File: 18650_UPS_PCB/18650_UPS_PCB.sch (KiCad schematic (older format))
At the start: 59 parts, among them J1 USB_B_Micro, J2 Conn_02x04_Odd_Even, J3 USB_A, SW1 SW_SPDT, SW2 ALPSALPINE_SKRHADE011, SW3 SW_SPDT, SW4 SW_SPDT, SW5 SW_SPDT, U1 STLINK-V3MINI, U10 LR9102G-xx, U2 R5478, U3 STC4054, U4 FS8205A, U5 ME2188Cxx, U6 XC9236Axx, U7 INA219AxD, U8 SSD1306_128_32, U9 STM32F030F4Px

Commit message: all components on board
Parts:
- removed TP1, TP2, TP3, TP4, TP5: TestPoint, TestPoint:TestPoint_Keystone_5015_Micro-Minature, symbol Connector:TestPoint
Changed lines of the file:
@@
 	6700 8300 6600 8300
-Wire Wire Line
-	6600 8950 6600 9000
 Wire Wire Line
 	6700 7900 6600 7900
@@
 Wire Wire Line
 	7300 5950 8200 5950
-Wire Wire Line
-	6600 9350 6600 9400
 $Comp
 L power:-BATT #PWR015
@@
 $EndComp
 $Comp
-L power:+5V #PWR027
-U 1 1 60E79ACF
-P 13350 5800
-AR Path="/60E79ACF" Ref="#PWR027"  Part="1"
-AR Path="/60952D5B/60E79ACF" Ref="#PWR?"  Part="1"
-F 0 "#PWR027" H 13350 5650 50  0001 C CNN
-F 1 "+5V" H 13365 5973 50  0000 C CNN
-F 2 "" H 13350 5800 50  0001 C CNN
-F 3 "" H 13350 5800 50  0001 C CNN
-	1    13350 5800
-	1    0    0    -1
-$EndComp
-$Comp
 L power:GNDD #PWR025
 U 1 1 60E79E71
@@
 	13250 5900 13350 5900
 Connection ~ 13350 5900
-Wire Wire Line
-	13350 5900 13350 5800
 $Comp
 L power:GNDD #PWR028
@@
 Wire Wire Line
 	12000 4100 12000 4000
-$Comp
-L power:+3V3 #PWR031
-U 1 1 60F8808E
-P 13900 3700
-AR Path="/60F8808E" Ref="#PWR031"  Part="1"
-AR Path="/60952D5B/60F8808E" Ref="#PWR?"  Part="1"
-F 0 "#PWR031" H 13900 3550 50  0001 C CNN
-F 1 "+3V3" H 13915 3873 50  0000 C CNN
-F 2 "" H 13900 3700 50  0001 C CNN
-F 3 "" H 13900 3700 50  0001 C CNN
-	1    13900 3700
-	1    0    0    -1
-$EndComp
 Wire Wire Line
 	13250 3950 13350 3950
@@
 Wire Wire Line
 	11950 7950 11950 7900
-$Comp
-L power:+3.3VA #PWR029
-U 1 1 6112D4E0
-P 13700 7850
-F 0 "#PWR029" H 13700 7700 50  0001 C CNN
-F 1 "+3.3VA" H 13715 8023 50  0000 C CNN
-F 2 "" H 13700 7850 50  0001 C CNN
-F 3 "" H 13700 7850 50  0001 C CNN
-	1    13700 7850
-	1    0    0    -1
-$EndComp
-Wire Wire Line
-	13700 7950 13700 7850
 Connection ~ 13700 7950
 Wire Notes Line
@@
 	1    0    0    -1
 $EndComp
-$Comp
-L Connector:TestPoint TP1
-U 1 1 60CA037D
-P 6900 8900
-F 0 "TP1" H 6958 9018 50  0000 L CNN
-F 1 "TestPoint" H 6958 8927 50  0000 L CNN
-F 2 "TestPoint:TestPoint_Keystone_5015_Micro-Minature" H 7100 8900 50  0001 C CNN
-F 3 "~" H 7100 8900 50  0001 C CNN
-	1    6900 8900
-	1    0    0    -1
-$EndComp
-$Comp
-L Connector:TestPoint TP2
-U 1 1 60CAD6BC
-P 6900 9350
-F 0 "TP2" H 6958 9468 50  0000 L CNN
-F 1 "TestPoint" H 6958 9377 50  0000 L CNN
-F 2 "TestPoint:TestPoint_Keystone_5015_Micro-Minature" H 7100 9350 50  0001 C CNN
-F 3 "~" H 7100 9350 50  0001 C CNN
-	1    6900 9350
-	1    0    0    -1
-$EndComp
-Wire Wire Line
-	6900 9350 6900 9400
-Wire Wire Line
-	6900 9400 6600 9400
-Connection ~ 6600 9400
-Wire Wire Line
-	6600 9400 6600 9450
-Wire Wire Line
-	6900 8900 6900 9000
-Wire Wire Line
-	6900 9000 6600 9000
-Connection ~ 6600 9000
-Wire Wire Line
-	6600 9000 6600 9050
-$Comp
-L Connector:TestPoint TP4
-U 1 1 60CC539E
-P 14000 7900
-F 0 "TP4" H 14058 8018 50  0000 L CNN
-F 1 "TestPoint" H 14058 7927 50  0000 L CNN
-F 2 "TestPoint:TestPoint_Keystone_5015_Micro-Minature" H 14200 7900 50  0001 C CNN
-F 3 "~" H 14200 7900 50  0001 C CNN
-	1    14000 7900
-	1    0    0    -1
-$EndComp
-Wire Wire Line
-	13700 7950 14000 7950
-Wire Wire Line
-	14000 7950 14000 7900
-$Comp
-L Connector:TestPoint TP3
-U 1 1 60CD1FDC
-P 13650 5850
-F 0 "TP3" H 13708 5968 50  0000 L CNN
-F 1 "TestPoint" H 13708 5877 50  0000 L CNN
-F 2 "TestPoint:TestPoint_Keystone_5015_Micro-Minature" H 13850 5850 50  0001 C CNN
-F 3 "~" H 13850 5850 50  0001 C CNN
-	1    13650 5850
-	1    0    0    -1
-$EndComp
-Wire Wire Line
-	13350 5900 13650 5900
-Wire Wire Line
-	13650 5900 13650 5850
-$Comp
-L Connector:TestPoint TP5
-U 1 1 60CDED71
-P 14150 3750
-F 0 "TP5" H 14208 3868 50  0000 L CNN
-F 1 "TestPoint" H 14208 3777 50  0000 L CNN
-F 2 "TestPoint:TestPoint_Keystone_5015_Micro-Minature" H 14350 3750 50  0001 C CNN
-F 3 "~" H 14350 3750 50  0001 C CNN
-	1    14150 3750
-	1    0    0    -1
-$EndComp
-Wire Wire Line
-	13900 3700 13900 3750
 Wire Wire Line
 	13650 3750 13900 3750
@@
 Wire Wire Line
 	13900 3750 13900 3800
-Wire Wire Line
-	13900 3750 14150 3750
 $Comp
 L Connector:USB_A J3
@@
 NoConn ~ 4150 10550
 NoConn ~ 2900 10450
-$Comp
-L power:+3.3VA #PWR?
+Wire Wire Line
+	13900 3700 13900 3750
+$Comp
+L power:+3V3 #PWR031
+U 1 1 60F8808E
+P 13900 3700
+AR Path="/60F8808E" Ref="#PWR031"  Part="1"
+AR Path="/60952D5B/60F8808E" Ref="#PWR?"  Part="1"
+F 0 "#PWR031" H 13900 3550 50  0001 C CNN
+F 1 "+3V3" H 13915 3873 50  0000 C CNN
+F 2 "" H 13900 3700 50  0001 C CNN
+F 3 "" H 13900 3700 50  0001 C CNN
+	1    13900 3700
+	1    0    0    -1
+$EndComp
+Wire Wire Line
+	13350 5900 13350 5800
+$Comp
+L power:+5V #PWR027
+U 1 1 60E79ACF
+P 13350 5800
+AR Path="/60E79ACF" Ref="#PWR027"  Part="1"
+AR Path="/60952D5B/60E79ACF" Ref="#PWR?"  Part="1"
+F 0 "#PWR027" H 13350 5650 50  0001 C CNN
+F 1 "+5V" H 13365 5973 50  0000 C CNN
+F 2 "" H 13350 5800 50  0001 C CNN
+F 3 "" H 13350 5800 50  0001 C CNN
+	1    13350 5800
+	1    0    0    -1
+$EndComp
+$Comp
+L power:+3.3VA #PWR0110
 U 1 1 61291B27
 P 2150 4850
-F 0 "#PWR?" H 2150 4700 50  0001 C CNN
+F 0 "#PWR0110" H 2150 4700 50  0001 C CNN
 F 1 "+3.3VA" H 2165 5023 50  0000 C CNN
 F 2 "" H 2150 4850 50  0001 C CNN
@@
 	1    0    0    -1
 $EndComp
+Wire Wire Line
+	13700 7950 13700 7850
+$Comp
+L power:+3.3VA #PWR029
+U 1 1 6112D4E0
+P 13700 7850
+F 0 "#PWR029" H 13700 7700 50  0001 C CNN
+F 1 "+3.3VA" H 13715 8023 50  0000 C CNN
+F 2 "" H 13700 7850 50  0001 C CNN
+F 3 "" H 13700 7850 50  0001 C CNN
+	1    13700 7850
+	1    0    0    -1
+$EndComp
+Wire Wire Line
+	6600 9350 6600 9450
+Wire Wire Line
+	6600 8950 6600 9050
 $EndSCHEMATC

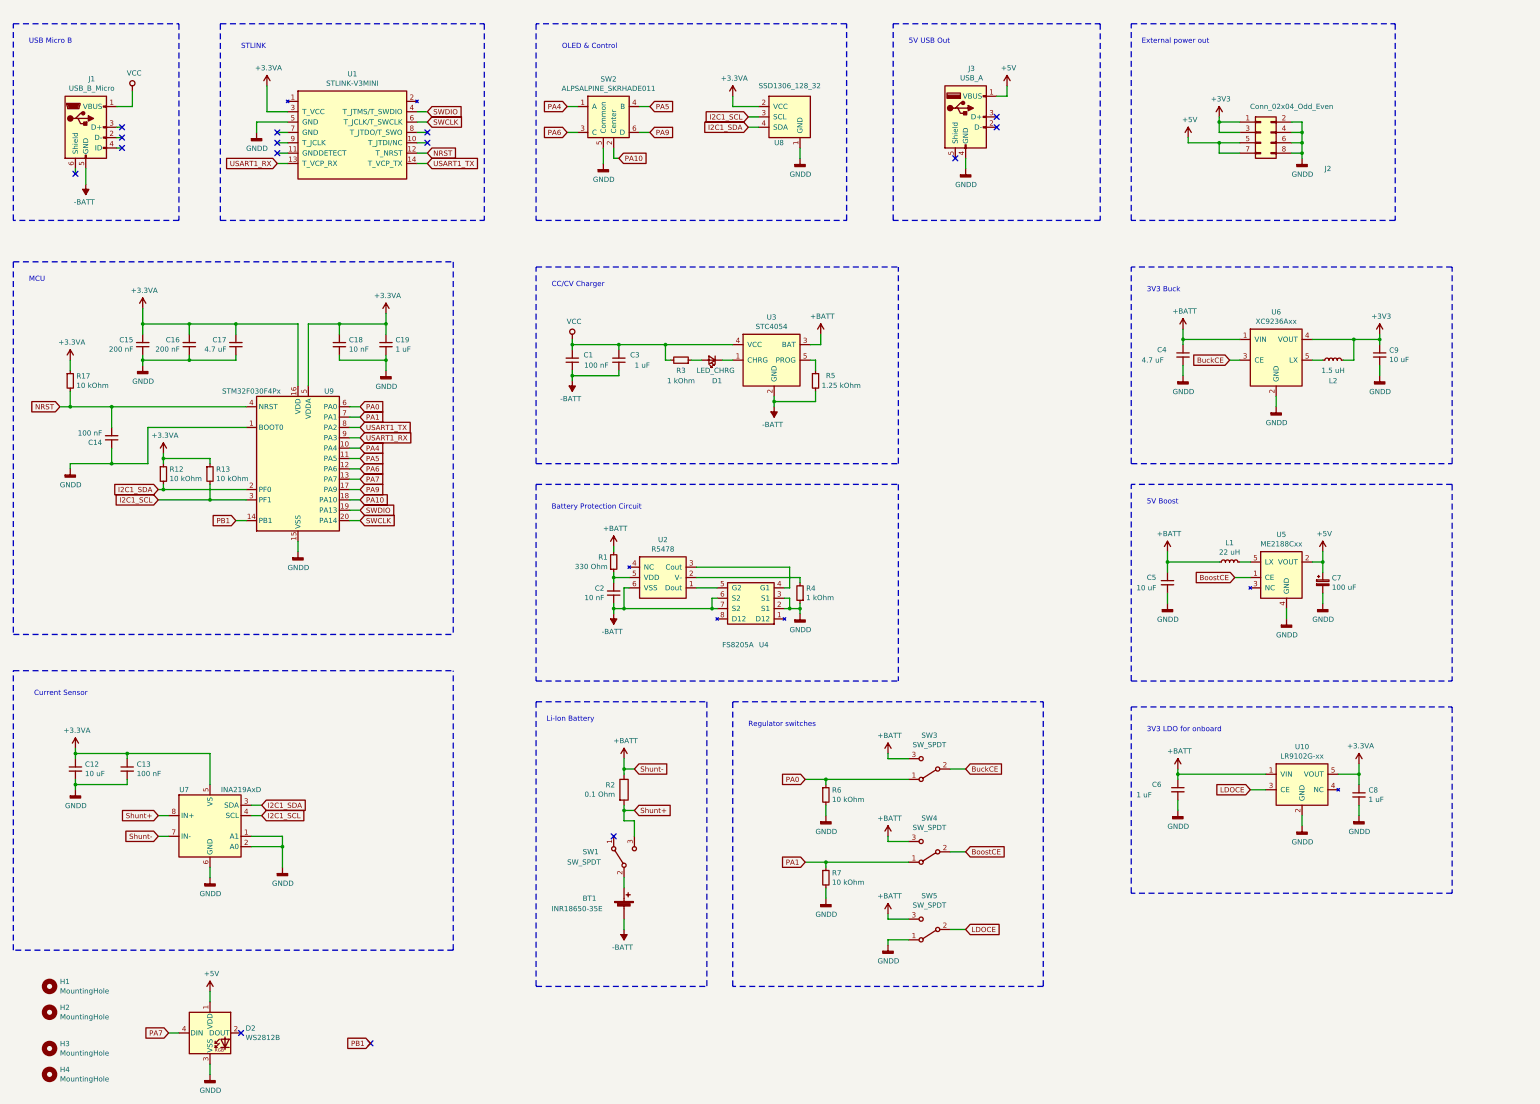
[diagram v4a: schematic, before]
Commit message: v2 layout complete and started routing
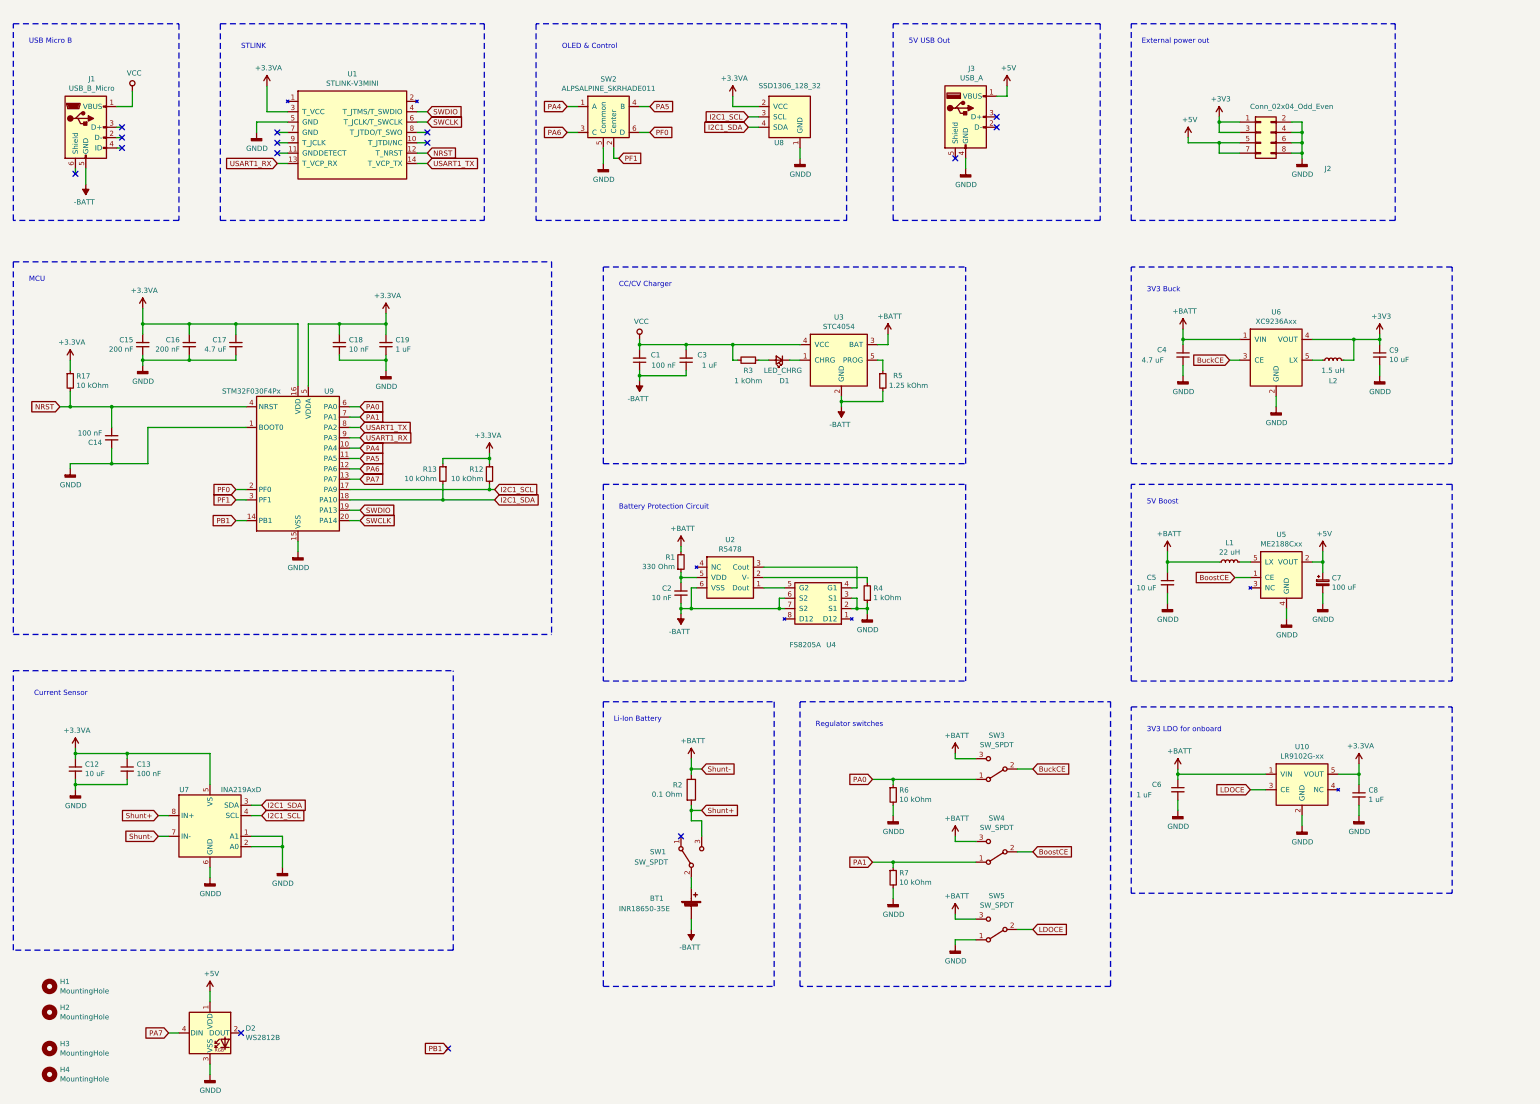
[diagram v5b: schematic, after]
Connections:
- net I2C1_SCL: now also R12.2, U9.17 (PA9); no longer R13.2, U9.3 (PF1)
- net I2C1_SDA: now also R13.2, U9.18 (PA10); no longer R12.2, U9.2 (PF0)
- net PA10 renamed PF1
- net PF1: now also U9.3 (PF1); no longer U9.18 (PA10)
- net PA9 renamed PF0
- net PF0: now also U9.2 (PF0); no longer U9.17 (PA9)
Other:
- moved on the sheet: BT1, C1, C2, C3, D1, R1, R12, R13, R2, R3, R4, R5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

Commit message: routing
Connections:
- net PA0: now also R7.1, SW4.1 (A); no longer R6.1, SW3.1 (A)
- net PA1: now also R6.1, SW3.1 (A); no longer R7.1, SW4.1 (A)
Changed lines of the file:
@@
 Text GLabel 6050 1750 0    50   Input ~ 0
 PA6
+Text GLabel 9000 8800 0    50   Input ~ 0
+PA0
 Text GLabel 9000 8000 0    50   Input ~ 0
-PA0
-Text GLabel 9000 8800 0    50   Input ~ 0
 PA1
 Text GLabel 10550 7900 2    50   Input ~ 0

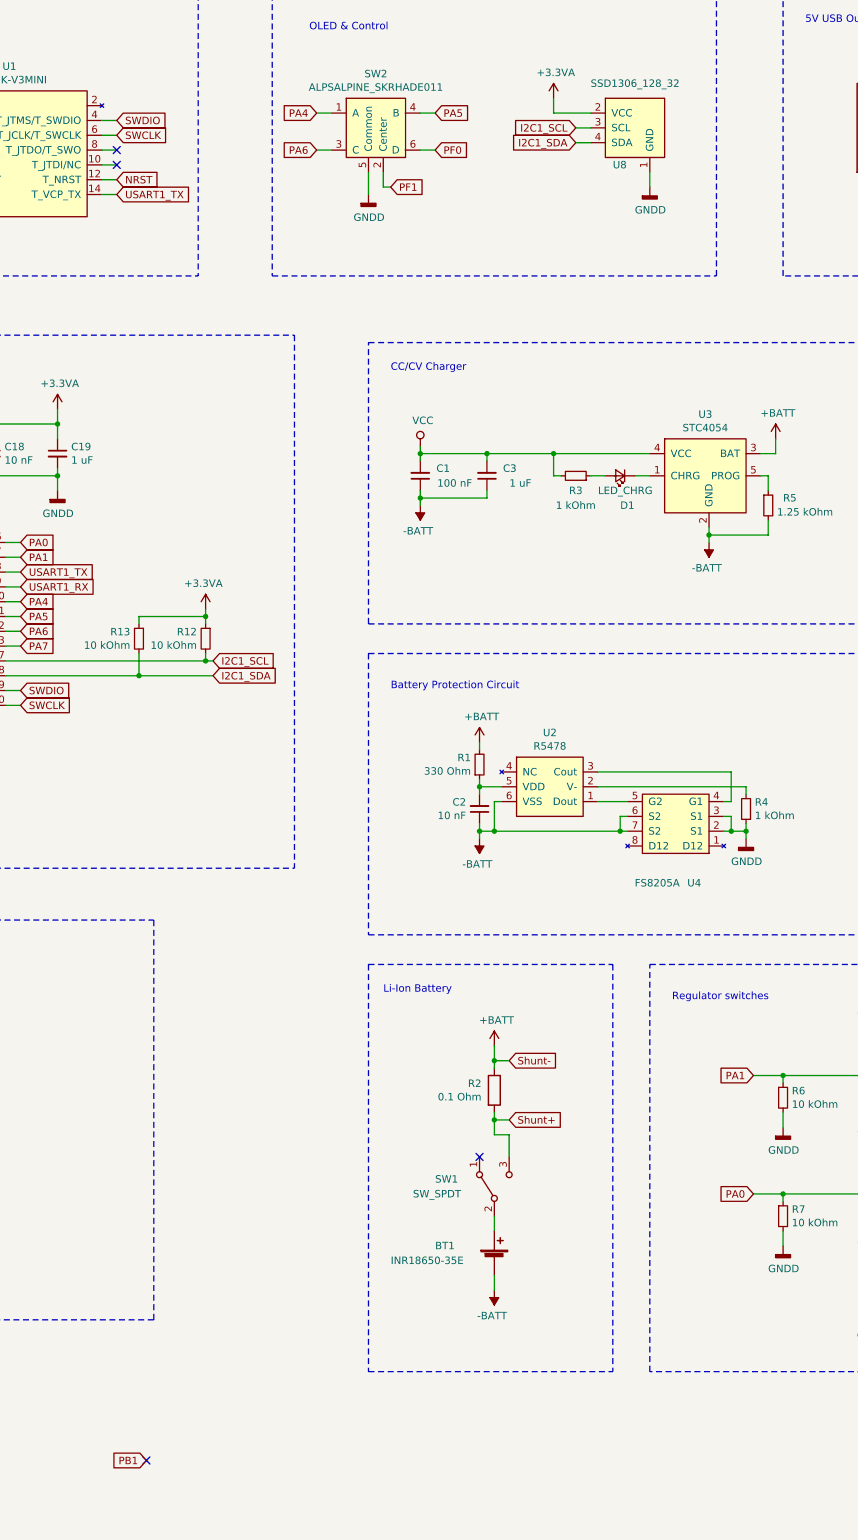
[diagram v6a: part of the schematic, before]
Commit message: cleaned routing significantly
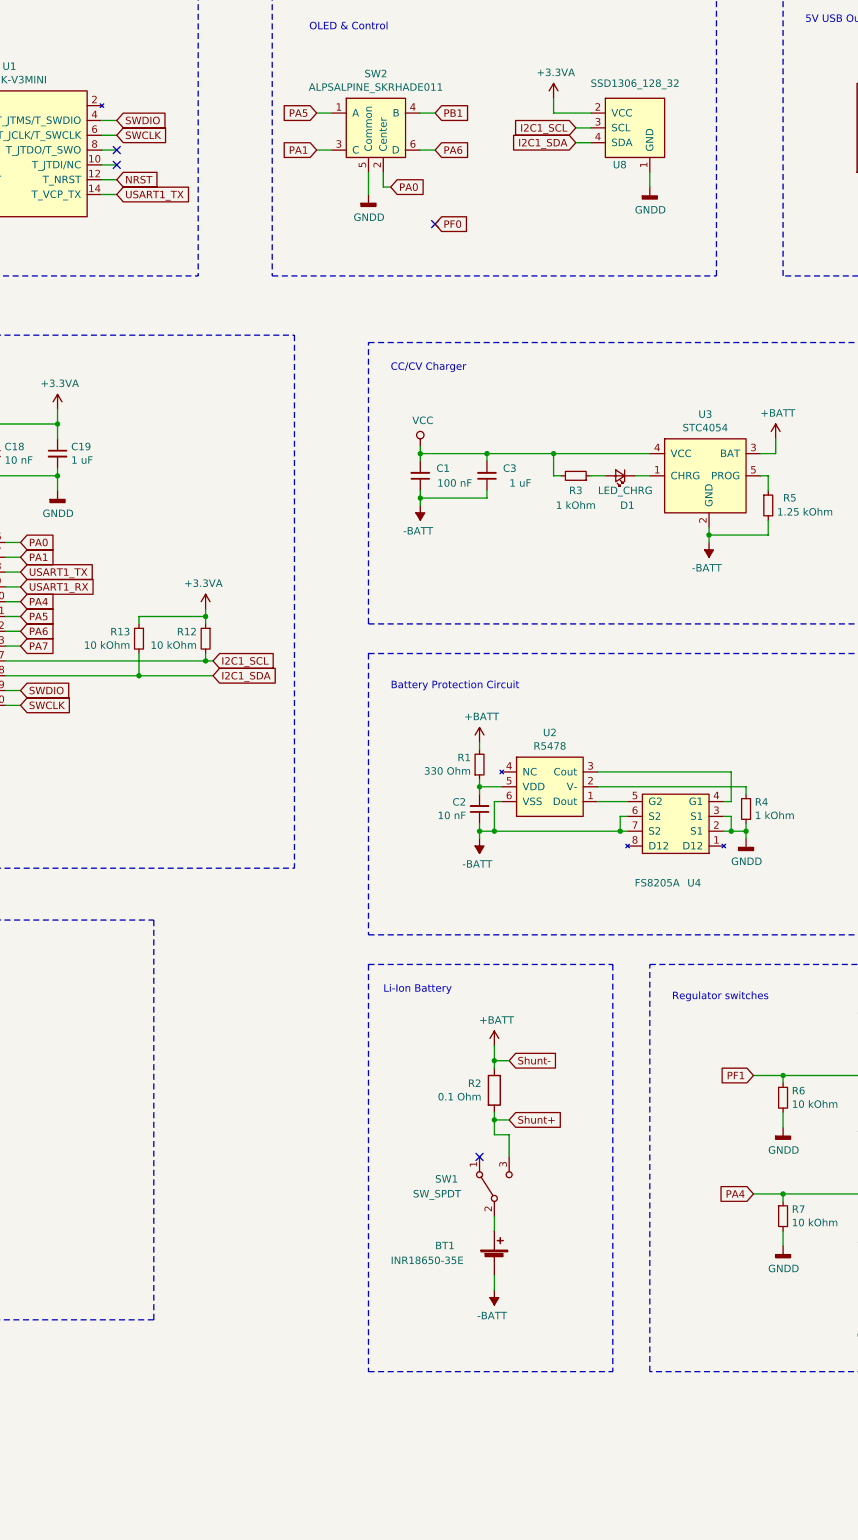
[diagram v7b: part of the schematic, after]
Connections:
- net PA0: now also SW2.2 (Center); no longer R7.1, SW4.1 (A)
- net PA1: now also SW2.3 (C); no longer R6.1, SW3.1 (A)
- net PA4: now also R7.1, SW4.1 (A); no longer SW2.1 (A)
- net PA5: now also SW2.1 (A); no longer SW2.4 (B)
- net PA6: now also SW2.6 (D); no longer SW2.3 (C)
- net PB1: now also SW2.4 (B)
- net PF0: no longer SW2.6 (D)
- net PF1: now also R6.1, SW3.1 (A); no longer SW2.2 (Center)
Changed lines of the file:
@@
 	-1   0    0    1
 $EndComp
+Text GLabel 9000 8800 0    50   Input ~ 0
+PA4
 Text GLabel 6050 1500 0    50   Input ~ 0
-PA4
-Text GLabel 6850 1500 2    50   Input ~ 0
 PA5
+Text GLabel 6850 1750 2    50   Input ~ 0
+PA6
+Text GLabel 6550 2000 2    50   Input ~ 0
+PA0
 Text GLabel 6050 1750 0    50   Input ~ 0
-PA6
-Text GLabel 9000 8800 0    50   Input ~ 0
-PA0
-Text GLabel 9000 8000 0    50   Input ~ 0
 PA1
 Text GLabel 10550 7900 2    50   Input ~ 0
@@
 Wire Wire Line
 	2850 5300 2950 5300
-Text GLabel 4900 10600 0    50   Input ~ 0
+Text GLabel 6850 1500 2    50   Input ~ 0
 PB1
-Text GLabel 6850 1750 2    50   Input ~ 0
+Text GLabel 6850 2250 2    50   Input ~ 0
 PF0
-Text GLabel 6550 2000 2    50   Input ~ 0
+Text GLabel 9000 8000 0    50   Input ~ 0
 PF1
-NoConn ~ 4900 10600
+NoConn ~ 6850 2250
 $EndSCHEMATC
